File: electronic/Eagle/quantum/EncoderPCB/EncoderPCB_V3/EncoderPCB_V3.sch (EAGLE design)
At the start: 31 parts, among them IC1 STM32F031K6T6, IC2 STM32F031K6T6

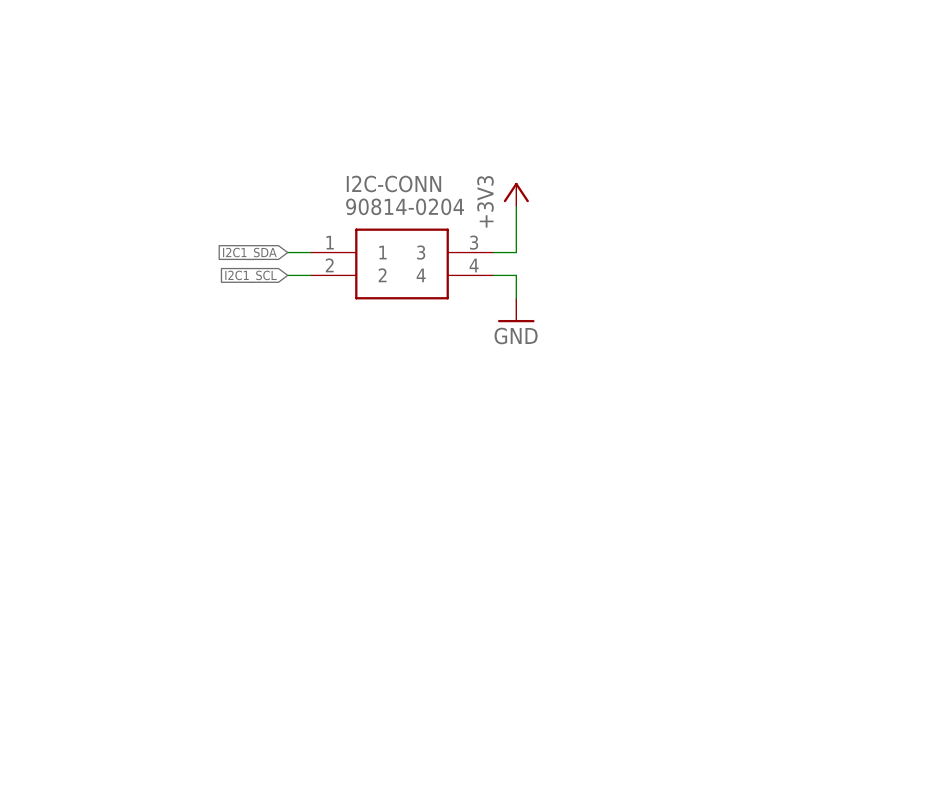
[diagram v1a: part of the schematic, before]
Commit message: started Plugin "klanghabitat connector"
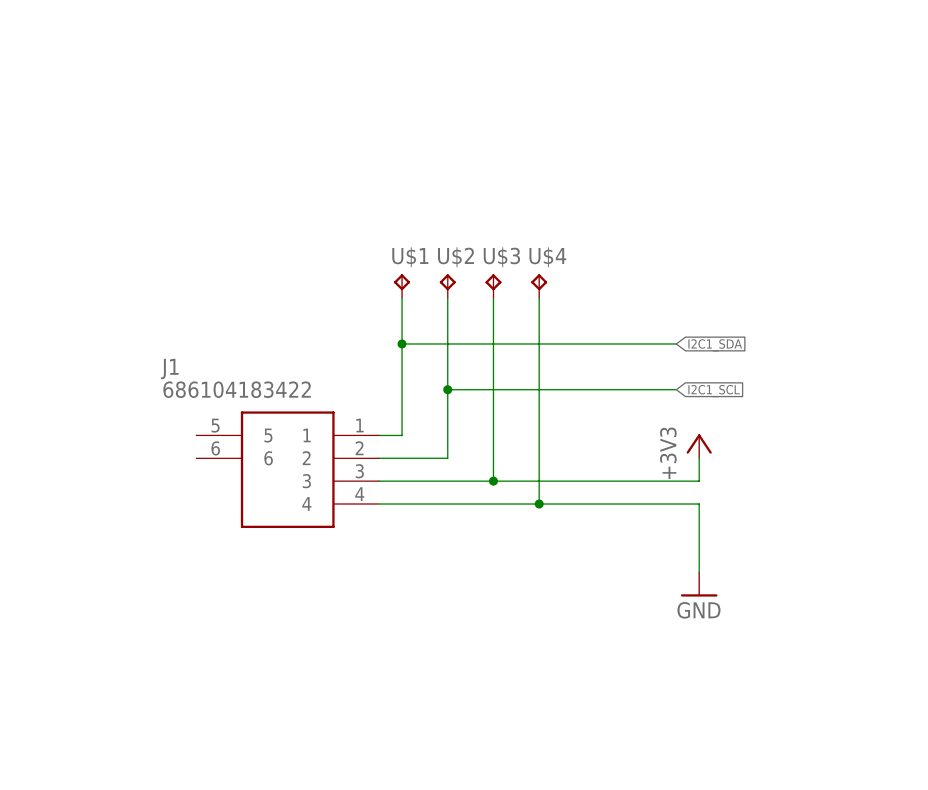
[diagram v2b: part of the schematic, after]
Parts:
- removed I2C-CONN: 90814-0204, electro_mechanical:90814-0204
- added J1: 686104183422, electro_mechanical:686104183422
- added U$1, U$2, U$3, U$4: TP, C_Sager_Bibliothek:TP
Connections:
- net +3V3: now also J1.3, U$3.TP; no longer I2C-CONN.3
- net GND: now also J1.4, U$4.TP; no longer I2C-CONN.4
- net I2C1_SCL: now also J1.2, U$2.TP; no longer I2C-CONN.2
- net I2C1_SDA: now also J1.1, U$1.TP; no longer I2C-CONN.1
